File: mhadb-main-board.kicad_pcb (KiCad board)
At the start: 2 copper layers, 60 x 50 mm, 106 parts, among them J1 Conn_01x04, J10 Conn_01x04_Pin, J2 Conn_01x04, J3 USB_C_Receptacle_USB2.0_14P, J4 Conn_01x02, J5 Conn_01x03, J6 Conn_01x03, J7 Conn_01x04, J8 Conn_01x04, J9 Conn_01x04_Pin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

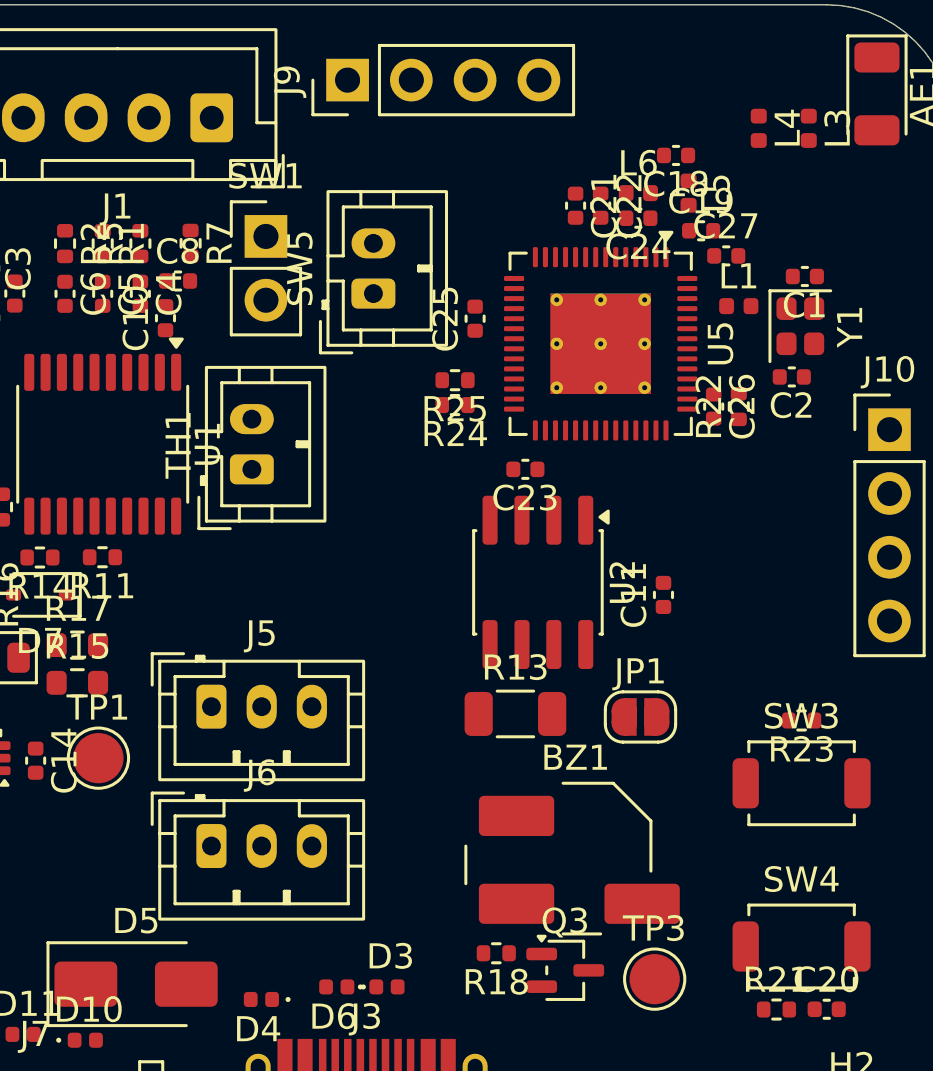
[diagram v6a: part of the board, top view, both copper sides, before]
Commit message: schem/pcb: add TMP117 temp sensor
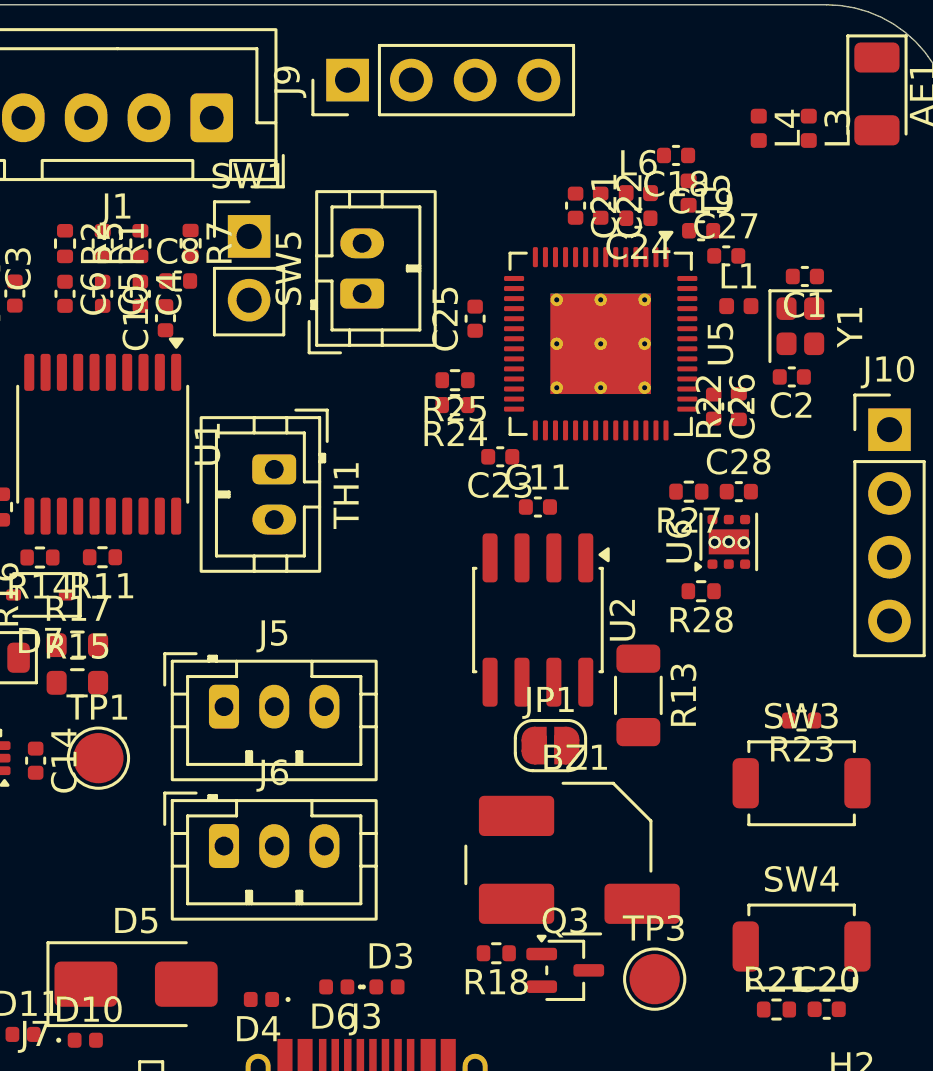
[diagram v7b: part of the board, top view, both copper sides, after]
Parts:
- added C28: 0u1, Capacitor_SMD:C_0402_1005Metric, F.Cu at (151.5, 69.4)
- added R27: 10k, Resistor_SMD:R_0402_1005Metric, F.Cu at (149.5, 69.4)
- added R28: 10k, Resistor_SMD:R_0402_1005Metric, F.Cu at (150.0, 73.4)
- added U6: TMP117AIDRV, Package_SON:WSON-6-1EP_2x2mm_P0.65mm_EP1x1.6mm, F.Cu at (151.1, 71.4)
- moved C11 6.10 mm to (143.5, 70.0), turned to 0 degrees
- moved R13 4.95 mm to (147.5, 77.5), turned to -90 degrees
- moved JP1 3.76 mm to (144.0, 79.5)
- moved U2 1.50 mm to (143.5, 74.5)
- moved C23 1.12 mm to (142.0, 68.0)
- moved TH1 0.89 mm to (133.0, 68.5), turned to -90 degrees
- moved SW1 0.67 mm to (132.0, 59.2)
- moved J5 0.50 mm to (131.0, 78.0)
- moved J6 0.50 mm to (131.0, 83.5)
- moved SW5 0.45 mm to (136.5, 61.5)
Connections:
- U5 pad 19: unconnected-(U5-GPIO14/ADC2_CH3-Pad19) -> /ALERT
- U5 pad 47: unconnected-(U5-MTDI/JTAG/GPIO41-Pad47) -> /SDA
- U5 pad 48: unconnected-(U5-MTMS/JTAG/GPIO42-Pad48) -> /SCL
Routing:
- net GND: vias 0 -> 3

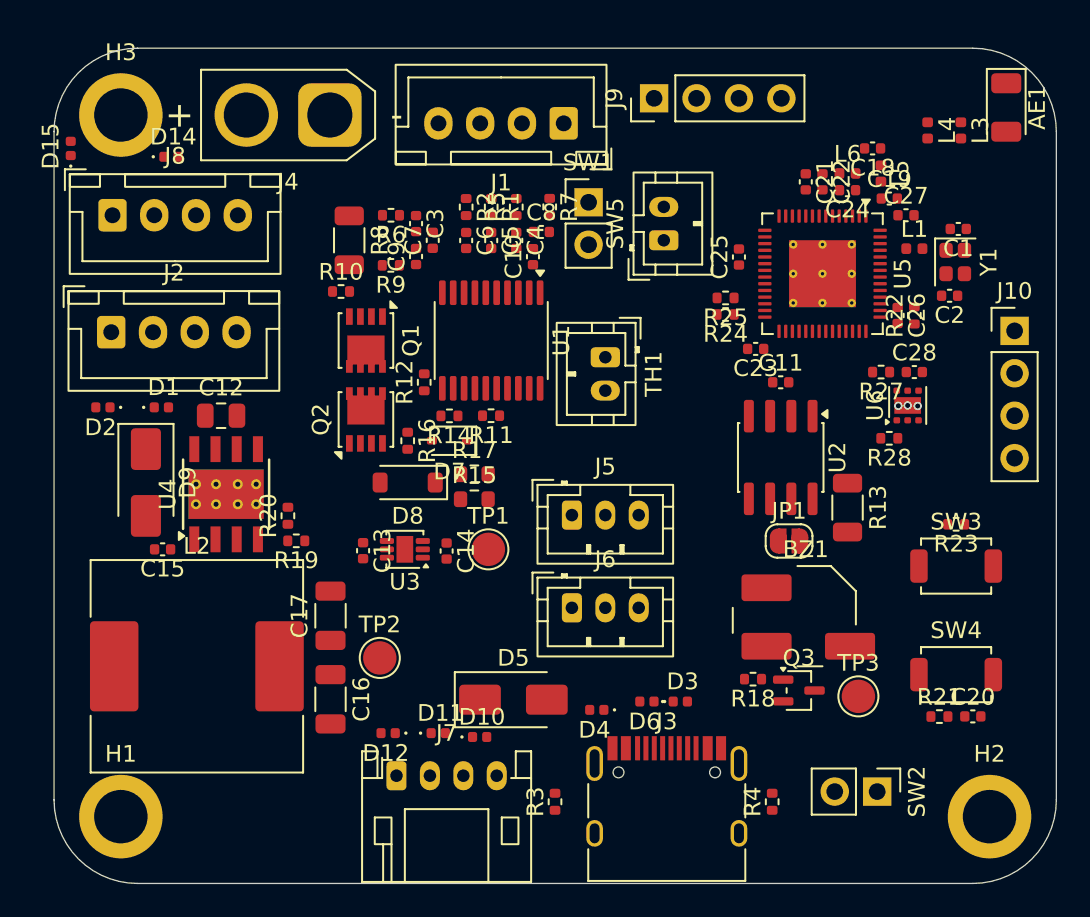
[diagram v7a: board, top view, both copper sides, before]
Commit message: pcb: changed outline to 50x50mm
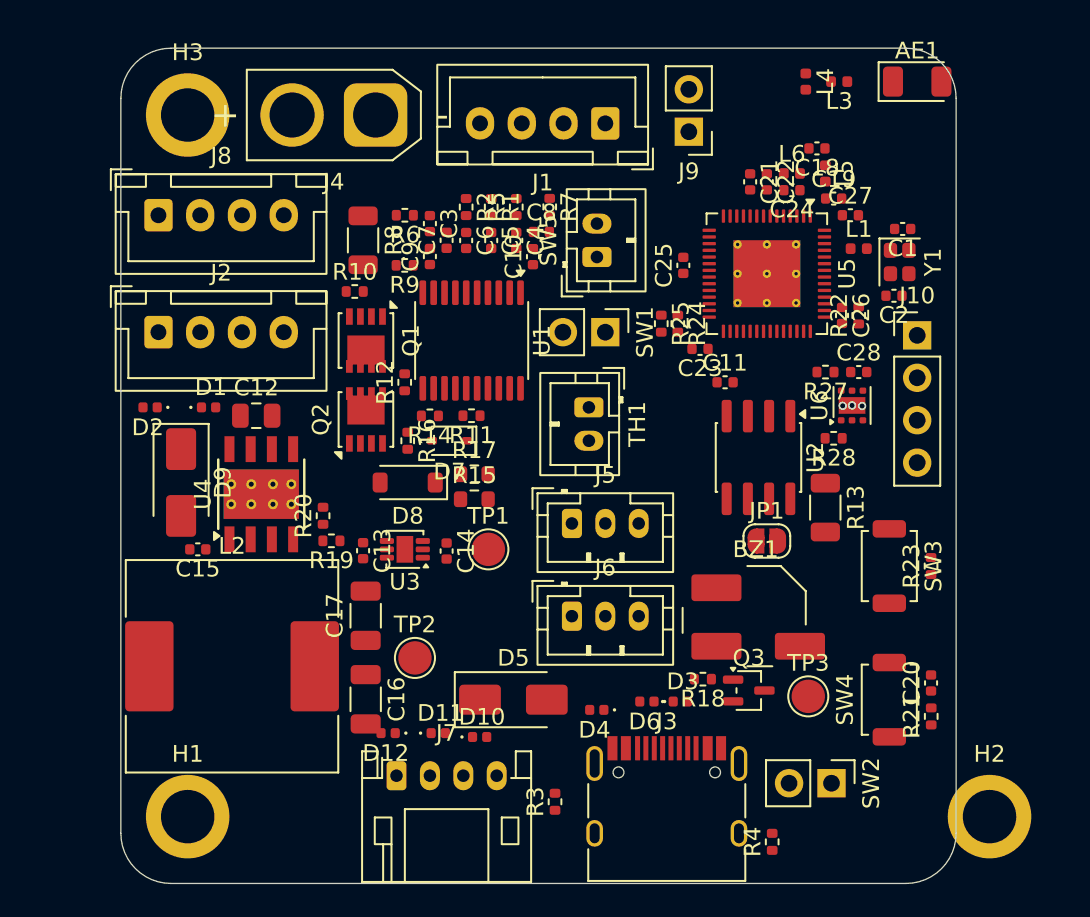
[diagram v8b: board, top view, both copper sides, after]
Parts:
- removed D14, D15: H5VU10U, GLCS:Diode_DFN1006
- J9: value Conn_01x04_Pin -> Conn_01x02_Pin; footprint Connector_PinHeader_2.54mm:PinHeader_1x04_P2.54mm_Vertical -> Connector_PinHeader_2.54mm:PinHeader_1x02_P2.54mm_Vertical
- moved L4 7.86 mm to (145.0, 52.0)
- moved L3 7.85 mm to (147.0, 52.0), turned to 180 degrees
- moved SW1 7.84 mm to (133.0, 67.0), turned to -90 degrees
- moved J10 5.84 mm to (151.7, 67.2)
- moved AE1 5.55 mm to (151.7, 52.0), turned to 0 degrees
- moved SW4 4.27 mm to (150.0, 89.0), turned to 90 degrees
- moved R25 4.15 mm to (136.3, 66.5), turned to -90 degrees
- moved SW5 4.12 mm to (132.5, 62.5)
- moved H1 4.00 mm to (108.0, 96.0)
- moved H3 4.00 mm to (108.0, 54.0)
- moved SW3 4.00 mm to (150.0, 81.0), turned to -90 degrees
- moved C25 3.37 mm to (137.7, 63.0)
- moved C11 3.33 mm to (140.2, 70.0)
- moved C18 3.33 mm to (145.7, 56.0)
- moved C19 3.33 mm to (146.7, 59.0)
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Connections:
- U5 pad 10: Net-(J9-Pin_4) -> Net-(J9-Pin_2)
- U5 pad 11: Net-(J9-Pin_3) -> Net-(J9-Pin_1)
- U5 pad 12: Net-(J9-Pin_2) -> unconnected-(U5-GPIO7/ADC1_CH6-Pad12)
- U5 pad 13: Net-(J9-Pin_1) -> unconnected-(U5-GPIO8/ADC1_CH7-Pad13)
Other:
- board size 60 x 50 mm -> 50 x 50 mm
